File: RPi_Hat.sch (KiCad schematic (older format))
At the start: 25 parts

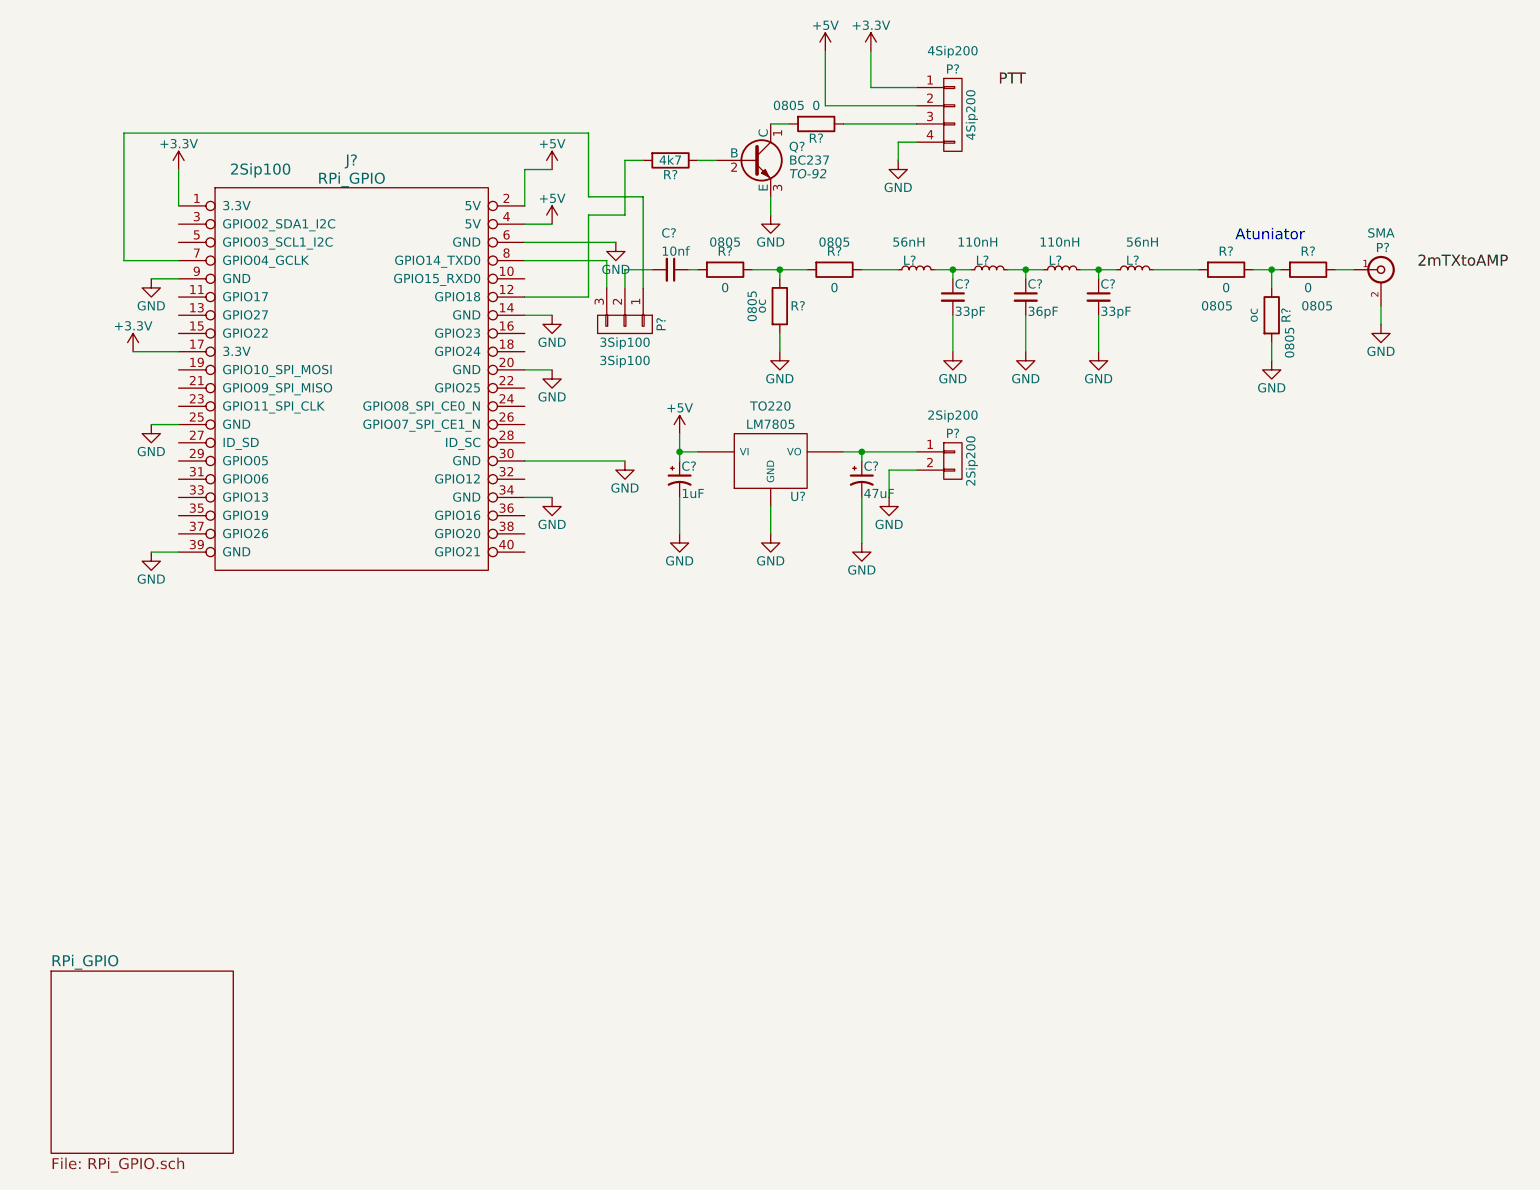
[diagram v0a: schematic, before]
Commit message: added annotation and module details
sma connector footprint still not corect
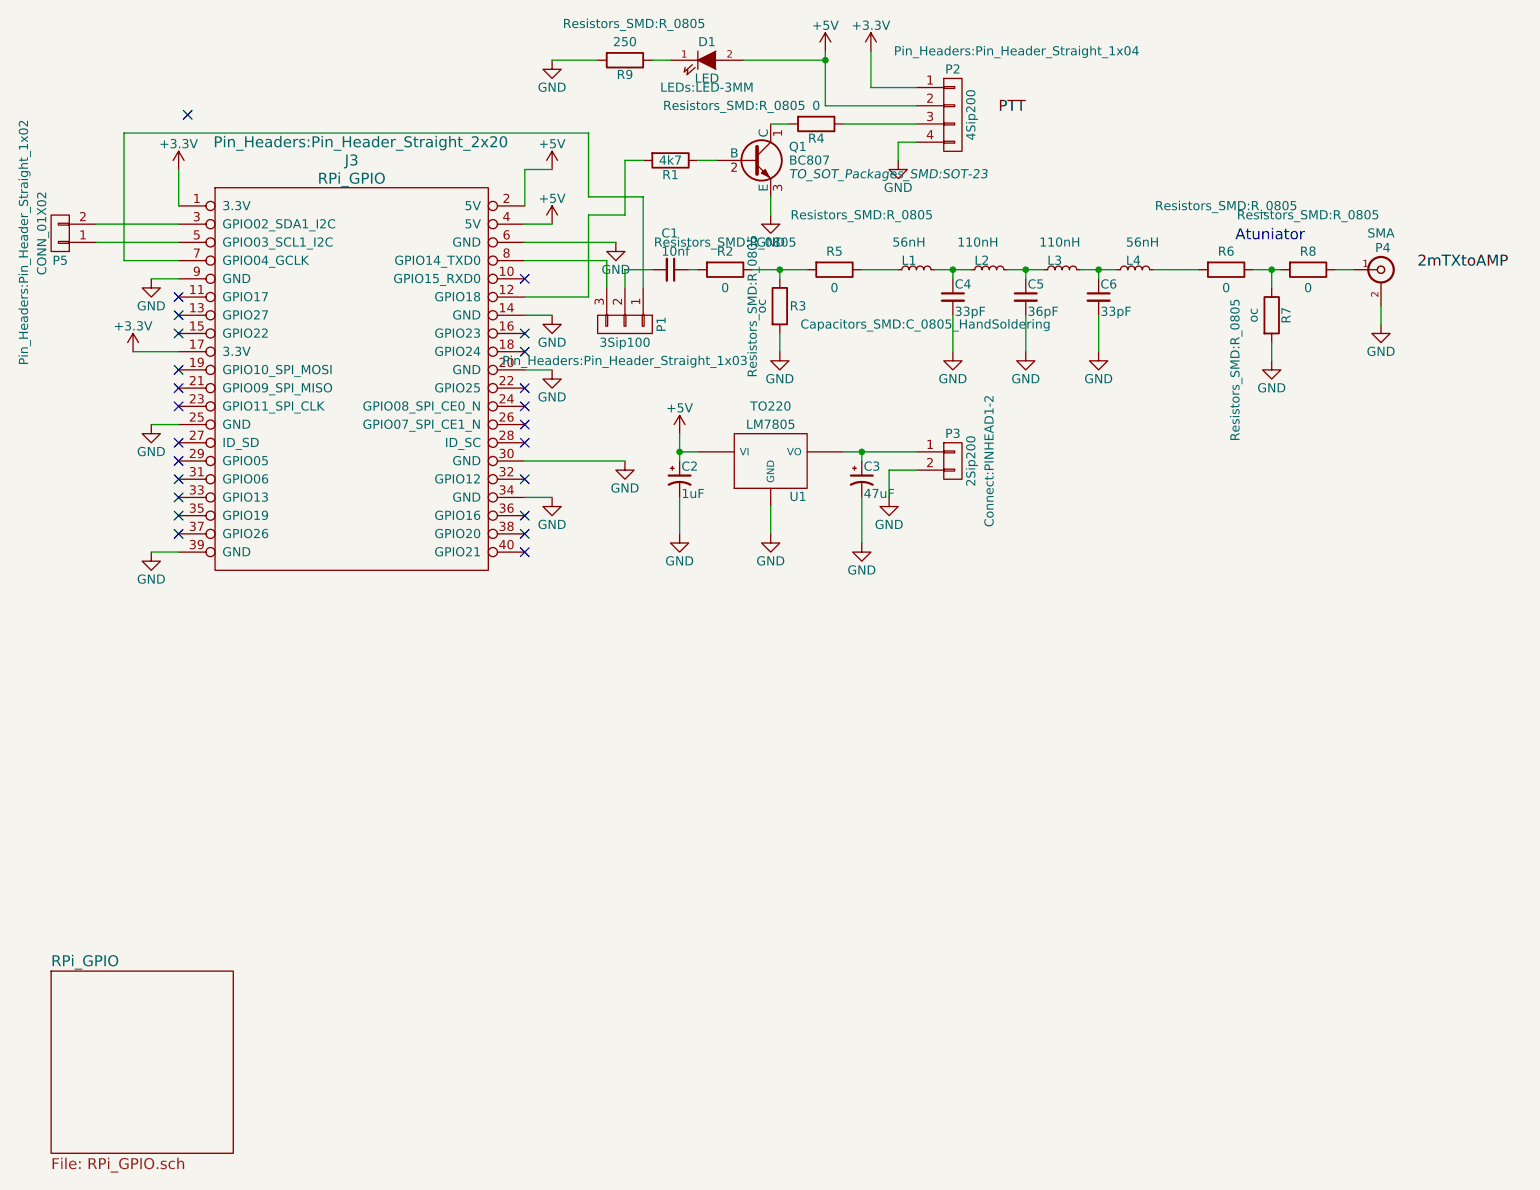
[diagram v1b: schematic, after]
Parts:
- added D1: LED, LEDs:LED-3MM, symbol LED
- added P5: CONN_01X02, Pin_Headers:Pin_Header_Straight_1x02, symbol CONN_01X02
- added R9: 250, Resistors_SMD:R_0805, symbol R
- C1, C5, C6: renamed from C?; footprint (none) -> Capacitors_SMD:C_0805
- C2: renamed from C?; footprint (none) -> Capacitors_SMD:c_elec_4x5.7
- C3: renamed from C?; footprint (none) -> Capacitors_SMD:c_elec_6.3x5.7
- C4: renamed from C?; footprint (none) -> Capacitors_SMD:C_0805_HandSoldering
- J3: renamed from J?; footprint 2Sip100 -> Pin_Headers:Pin_Header_Straight_2x20
- L1, L2, L3, L4: renamed from L?; footprint (none) -> Capacitors_SMD:C_0805_HandSoldering
- P1: renamed from P?; footprint 3Sip100 -> Pin_Headers:Pin_Header_Straight_1x03
- P2: renamed from P?; footprint 4Sip200 -> Pin_Headers:Pin_Header_Straight_1x04
- P3: renamed from P?; footprint 2Sip200 -> Connect:PINHEAD1-2
- Q1: renamed from Q?; value BC237 -> BC807; footprint TO-92 -> TO_SOT_Packages_SMD:SOT-23
- R1: renamed from R?; footprint (none) -> Resistors_SMD:R_0805
- R2, R3, R4, R5, R6, R7, R8: renamed from R?; footprint 0805 -> Resistors_SMD:R_0805
- gave numbers to parts that had none: 2
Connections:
- net +5V: now also D1.2 (A)
- net GND: now also R9.2
- net at J3.3 (GPIO02_SDA1_I2C): now also P5.2 (P2)
- net at J3.5 (GPIO03_SCL1_I2C): now also P5.1 (P1)
- new net: D1.1 (K), R9.1
- no-connect marks 0 -> 24

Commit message: Created SMA footprint and started laying out board
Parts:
- removed P4: SMA, symbol BNC
- added P4: SMA, Bacar:SMA_Edge, symbol SMA
- P2: footprint Pin_Headers:Pin_Header_Straight_1x04 -> Connect:AK300-4
- U1: footprint TO220 -> Power_Integrations:TO-220
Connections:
- net +5V: now also U1.VO; no longer U1.VI
- net GND: now also P4.2
- net at R8.1: now also P4.1
- net at C3.1, P3.1 (P1): now also U1.VI; no longer U1.VO
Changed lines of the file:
@@
 LIBS:valves
 LIBS:RPi_Hat-cache
+LIBS:SMA
 EELAYER 25 0
 EELAYER END
 $Descr A4 11693 8268
 encoding utf-8
-Sheet 1 2
+Sheet 1 1
 Title ""
 Date ""
@@
 Comment4 ""
 $EndDescr
-$Sheet
-S 900  5900 1000 1000
-U 5515D395
-F0 "RPi_GPIO" 60
-F1 "RPi_GPIO.sch" 60
-$EndSheet
 $Comp
 L RPi_GPIO J3
@@
 $EndComp
 $Comp
-L BNC P4
-U 1 1 5873BD61
-P 8200 2050
-F 0 "P4" H 8210 2170 50  0000 C CNN
-F 1 "SMA" H 8200 2250 50  0000 C CNN
-F 2 "" H 8200 2050 50  0001 C CNN
-F 3 "" H 8200 2050 50  0000 C CNN
-	1    8200 2050
-	1    0    0    -1
-$EndComp
-$Comp
 L GND #PWR04
 U 1 1 5873BE4D
@@
 F 0 "P2" H 5850 1450 50  0000 C CNN
 F 1 "4Sip200" V 5950 1200 50  0000 C CNN
-F 2 "Pin_Headers:Pin_Header_Straight_1x04" H 6200 1550 50  0000 C CNN
+F 2 "Connect:AK300-4" H 6200 1550 50  0000 C CNN
 F 3 "" H 5850 1200 50  0000 C CNN
 	1    5850 1200
@@
 Text Label 6100 1200 0    60   ~ 0
 PTT
-Text Label 8400 2050 0    60   ~ 0
+Text Label 8400 2100 0    60   ~ 0
 2mTXtoAMP
 $Comp
@@
 F 3 "" H 5350 3200 50  0000 C CNN
 	1    5350 3200
-	1    0    0    -1
-$EndComp
-$Comp
-L LM7805 U1
-U 1 1 5874847B
-P 4850 3100
-F 0 "U1" H 5000 2904 50  0000 C CNN
-F 1 "LM7805" H 4850 3300 50  0000 C CNN
-F 2 "TO220" H 4850 3400 50  0000 C CNN
-F 3 "" H 4850 3100 50  0000 C CNN
-	1    4850 3100
 	1    0    0    -1
 $EndComp
@@
 	7600 2150 7600 2050
 Connection ~ 7600 2050
-Wire Wire Line
-	8200 2250 8200 2350
 Wire Wire Line
 	7600 2450 7600 2550
@@
 NoConn ~ 3500 2100
 NoConn ~ 1650 1200
+$Comp
+L LM7805 U1
+U 1 1 5874847B
+P 4850 3100
+F 0 "U1" H 5000 2904 50  0000 C CNN
+F 1 "LM7805" H 4850 3300 50  0000 C CNN
+F 2 "Power_Integrations:TO-220" H 5000 3400 50  0000 C CNN
+F 3 "" H 4850 3100 50  0000 C CNN
+	1    4850 3100
+	-1   0    0    -1
+$EndComp
+$Comp
+L SMA P4
+U 1 1 587D7F9F
+P 8200 2050
+F 0 "P4" H 8280 2050 40  0000 L CNN
+F 1 "SMA" H 8200 2105 30  0001 C TNN
+F 2 "Bacar:SMA_Edge" H 8550 1900 60  0000 C CNN
+F 3 "" H 8200 2050 60  0000 C CNN
+	1    8200 2050
+	1    0    0    -1
+$EndComp
+Wire Wire Line
+	8200 2350 8200 2250
+Wire Wire Line
+	8200 2250 8050 2250
+Wire Wire Line
+	8050 2250 8050 2100
 $EndSCHEMATC

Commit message: Change Regulator transistor and connectors
Change Regulator transistor and connectors
Started laying out PCB
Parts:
- removed Q1: BC807, TO_SOT_Packages_SMD:SOT-23, symbol BC237
- added Q1: BC817-40, TO_SOT_Packages_SMD:SOT-23, symbol BC817-40
- C1, C5, C6: footprint Capacitors_SMD:C_0805 -> Capacitors_SMD:C_0805_HandSoldering
- P2: footprint Connect:AK300-4 -> Terminal_Blocks:TerminalBlock_Pheonix_MKDS1.5-4pol
- P3: footprint Connect:PINHEAD1-2 -> Terminal_Blocks:TerminalBlock_Pheonix_MKDS1.5-2pol
- R1, R2, R3, R4, R5, R6, R7, R8, R9: footprint Resistors_SMD:R_0805 -> Resistors_SMD:R_0805_HandSoldering
- U1: value LM7805 -> L4940V5 1.5A; symbol LM7805 -> LM7805-RESCUE-RPi_Hat
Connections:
- net +5V: now also U1.3 (VO); no longer U1.VO
- net GND: now also U1.2 (GND), Q1.2 (E); no longer U1.GND
- net at R4.2: now also Q1.3 (C)
- net at R1.1: now also Q1.1 (B)
- net at C3.1, P3.1 (P1): now also U1.1 (VI); no longer U1.VI
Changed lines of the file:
@@
 EESchema Schematic File Version 2
+LIBS:RPi_Hat-rescue
 LIBS:power
 LIBS:device
@@
 F 0 "C1" V 4100 2000 50  0000 L CNN
 F 1 "10nf" V 4200 2000 50  0000 L CNN
-F 2 "Capacitors_SMD:C_0805" H 4300 2050 50  0001 C CNN
+F 2 "Capacitors_SMD:C_0805_HandSoldering" H 4300 2050 50  0001 C CNN
 F 3 "" H 4300 2050 50  0000 C CNN
 	1    4300 2050
@@
 F 0 "R3" H 5000 2250 50  0000 C CNN
 F 1 "oc" V 4800 2250 50  0000 C CNN
-F 2 "Resistors_SMD:R_0805" V 4750 2250 50  0000 C CNN
+F 2 "Resistors_SMD:R_0805_HandSoldering" V 4750 2250 50  0000 C CNN
 F 3 "" H 4900 2250 50  0000 C CNN
 	1    4900 2250
@@
 F 0 "R2" V 4500 2050 50  0000 C CNN
 F 1 "0" V 4700 2050 50  0000 C CNN
-F 2 "Resistors_SMD:R_0805" V 4450 2050 50  0000 C CNN
+F 2 "Resistors_SMD:R_0805_HandSoldering" V 4450 2050 50  0000 C CNN
 F 3 "" H 4600 2050 50  0000 C CNN
 	1    4600 2050
@@
 F 0 "R5" V 5100 2050 50  0000 C CNN
 F 1 "0" V 5300 2050 50  0000 C CNN
-F 2 "Resistors_SMD:R_0805" V 4900 2200 50  0000 C CNN
+F 2 "Resistors_SMD:R_0805_HandSoldering" V 4900 2200 50  0000 C CNN
 F 3 "" H 5200 2050 50  0000 C CNN
 	1    5200 2050
@@
 F 0 "C5" H 6260 2270 50  0000 L CNN
 F 1 "36pF" H 6260 2120 50  0000 L CNN
-F 2 "Capacitors_SMD:C_0805" H 6250 2200 50  0001 C CNN
+F 2 "Capacitors_SMD:C_0805_HandSoldering" H 6250 2200 50  0001 C CNN
 F 3 "" H 6250 2200 50  0000 C CNN
 	1    6250 2200
@@
 F 0 "R6" V 7250 2050 50  0000 C CNN
 F 1 "0" V 7450 2050 50  0000 C CNN
-F 2 "Resistors_SMD:R_0805" V 7000 2050 50  0000 C CNN
+F 2 "Resistors_SMD:R_0805_HandSoldering" V 7000 2050 50  0000 C CNN
 F 3 "" H 7350 2050 50  0000 C CNN
 	1    7350 2050
@@
 F 0 "R8" V 7700 2050 50  0000 C CNN
 F 1 "0" V 7900 2050 50  0000 C CNN
-F 2 "Resistors_SMD:R_0805" V 7500 2050 50  0000 C CNN
+F 2 "Resistors_SMD:R_0805_HandSoldering" V 7500 2050 50  0000 C CNN
 F 3 "" H 7800 2050 50  0000 C CNN
 	1    7800 2050
@@
 F 0 "R7" V 7680 2300 50  0000 C CNN
 F 1 "oc" V 7500 2300 50  0000 C CNN
-F 2 "Resistors_SMD:R_0805" V 7400 2000 50  0000 C CNN
+F 2 "Resistors_SMD:R_0805_HandSoldering" V 7400 2000 50  0000 C CNN
 F 3 "" H 7600 2300 50  0000 C CNN
 	1    7600 2300
@@
 $EndComp
 $Comp
-L BC237 Q1
-U 1 1 5873C50C
-P 4750 1450
-F 0 "Q1" H 4950 1525 50  0000 L CNN
-F 1 "BC807" H 4950 1450 50  0000 L CNN
-F 2 "TO_SOT_Packages_SMD:SOT-23" H 4950 1375 50  0000 L CIN
-F 3 "" H 4750 1450 50  0000 L CNN
-	1    4750 1450
-	1    0    0    -1
-$EndComp
-$Comp
 L GND #PWR012
 U 1 1 5873C553
@@
 F 0 "R1" V 4380 1450 50  0000 C CNN
 F 1 "4k7" V 4300 1450 50  0000 C CNN
-F 2 "Resistors_SMD:R_0805" V 4230 1450 50  0001 C CNN
+F 2 "Resistors_SMD:R_0805_HandSoldering" V 4230 1450 50  0001 C CNN
 F 3 "" H 4300 1450 50  0000 C CNN
 	1    4300 1450
@@
 F 0 "R4" V 5180 1250 50  0000 C CNN
 F 1 "0" V 5000 1250 50  0000 C CNN
-F 2 "Resistors_SMD:R_0805" V 5000 800 50  0000 C CNN
+F 2 "Resistors_SMD:R_0805_HandSoldering" V 5000 800 50  0000 C CNN
 F 3 "" H 5100 1250 50  0000 C CNN
 	1    5100 1250
@@
 F 0 "P2" H 5850 1450 50  0000 C CNN
 F 1 "4Sip200" V 5950 1200 50  0000 C CNN
-F 2 "Connect:AK300-4" H 6200 1550 50  0000 C CNN
+F 2 "Terminal_Blocks:TerminalBlock_Pheonix_MKDS1.5-4pol" H 6200 1550 50  0000 C CNN
 F 3 "" H 5850 1200 50  0000 C CNN
 	1    5850 1200
@@
 F 0 "P3" H 5850 3250 50  0000 C CNN
 F 1 "2Sip200" V 5950 3100 50  0000 C CNN
-F 2 "Connect:PINHEAD1-2" V 6050 3100 50  0000 C CNN
+F 2 "Terminal_Blocks:TerminalBlock_Pheonix_MKDS1.5-2pol" V 6050 3100 50  0000 C CNN
 F 3 "" H 5850 3100 50  0000 C CNN
 	1    5850 3100
@@
 F 0 "C6" H 6660 2270 50  0000 L CNN
 F 1 "33pF" H 6660 2120 50  0000 L CNN
-F 2 "Capacitors_SMD:C_0805" H 6650 2200 50  0001 C CNN
+F 2 "Capacitors_SMD:C_0805_HandSoldering" H 6650 2200 50  0001 C CNN
 F 3 "" H 6650 2200 50  0000 C CNN
 	1    6650 2200
@@
 F 0 "R9" V 4130 900 50  0000 C CNN
 F 1 "250" V 3950 900 50  0000 C CNN
-F 2 "Resistors_SMD:R_0805" V 3850 950 50  0000 C CNN
+F 2 "Resistors_SMD:R_0805_HandSoldering" V 3850 950 50  0000 C CNN
 F 3 "" H 4050 900 50  0000 C CNN
 	1    4050 900
@@
 NoConn ~ 1650 1200
 $Comp
-L LM7805 U1
+L LM7805-RESCUE-RPi_Hat U1
 U 1 1 5874847B
 P 4850 3100
 F 0 "U1" H 5000 2904 50  0000 C CNN
-F 1 "LM7805" H 4850 3300 50  0000 C CNN
+F 1 "L4940V5  1.5A" H 4850 3300 50  0000 C CNN
 F 2 "Power_Integrations:TO-220" H 5000 3400 50  0000 C CNN
 F 3 "" H 4850 3100 50  0000 C CNN
@@
 Wire Wire Line
 	8050 2250 8050 2100
+$Comp
+L BC817-40 Q1
+U 1 1 58890E81
+P 4750 1450
+F 0 "Q1" H 4950 1525 50  0000 L CNN
+F 1 "BC817-40" H 4950 1450 50  0000 L CNN
+F 2 "TO_SOT_Packages_SMD:SOT-23" H 4950 1375 50  0000 L CIN
+F 3 "" H 4750 1450 50  0000 L CNN
+	1    4750 1450
+	1    0    0    -1
+$EndComp
 $EndSCHEMATC
